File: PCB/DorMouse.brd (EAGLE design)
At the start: 40.9 x 69.4 mm, 56 parts, among them IC1 LM340MP-05, IC2 MAX1551, U1 STM32F10XRXT6, X1 MINI-USB-UX60-MB-5ST

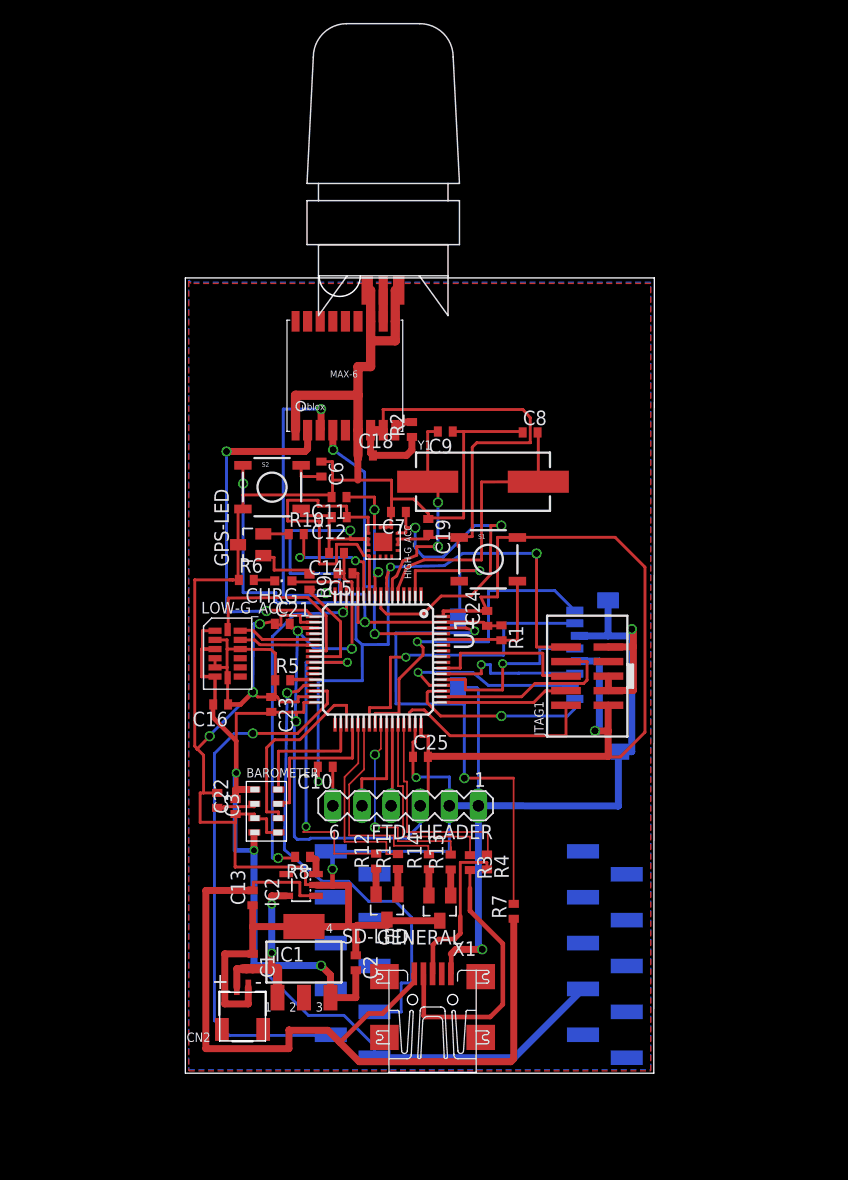
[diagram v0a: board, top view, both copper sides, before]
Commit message: Silkscreen work: values and mice
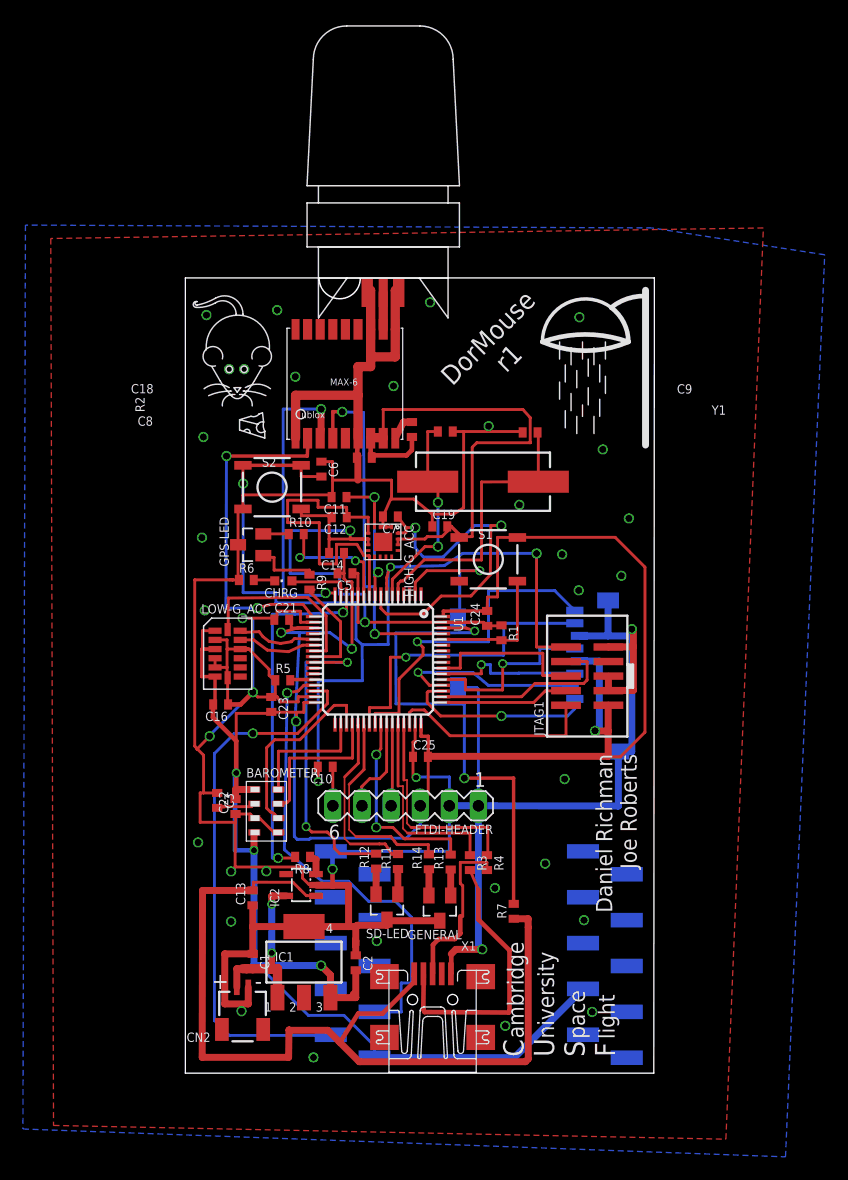
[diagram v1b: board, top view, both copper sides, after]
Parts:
- added U$2: (no value), DorMouse:SHOWER
- added U$3: (no value), DorMouse:DORMOUSE
- BAROMETER: device Swallow:LGA-8 -> DorMouse:LGA-8
- HIGH-G_ACC: device Swallow:LFCSP-16 -> DorMouse:LFCSP-16
- moved C19 1.00 mm to (22.2, 47.7), turned to 0 degrees
- moved C7 0.81 mm to (17.9, 48.6)
- moved GPS 0.70 mm to (14.0, 60.3)
- moved C21 0.36 mm to (8.41, 39.6)
- moved C18 0.22 mm to (15.6, 53.7)
- moved U$1 0.20 mm to (17.3, 68.1)
- moved R4 0.06 mm to (26.3, 18.4)
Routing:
- net TIMEPULSE: track 26.1 -> 31.2 mm
- net RESET: track 81.5 -> 86.6 mm
- net USB-5V: track 76.7 -> 81.0 mm
- net VCC: track 307.3 -> 311.0 mm
- net GND: track 382.5 -> 386.2 mm, vias 9 -> 38
- net SD_:): track 30.1 -> 28.6 mm
- net SERGEANT_SAD_FACE: track 18.8 -> 17.4 mm
- net CHARGING(-): track 30.1 -> 31.3 mm
- net ADC2: track 13.3 -> 14.4 mm
- net U1-TX: track 9.25 -> 8.48 mm
- net U2-TX: track 26.2 -> 26.9 mm
- net N$6: track 18.9 -> 18.3 mm
- net SD_:(: track 16.5 -> 15.9 mm
- net SD-DET: track 13.8 -> 13.2 mm
- net N$15: track 1.74 -> 2.32 mm
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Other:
- board text added: "C U S F"
- board text added: "Daniel Richman Joe Roberts"
- board text added: "DorMouse r1"
- board text added: "ambridge"
- board text added: "light"
- board text added: "niversity"
- board text added: "pace"

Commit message: CUSF Logo
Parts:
- added U$4: (no value), jonsowman:CUSF_LOGO
- moved R7 6.07 mm to (28.6, 20.2)
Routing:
- net N$21: track 43.7 -> 37.6 mm
- net USB-5V: track 81.0 -> 86.0 mm
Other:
- board text removed: "C U S F"
- board text removed: "ambridge"
- board text removed: "light"
- board text removed: "niversity"
- board text removed: "pace"
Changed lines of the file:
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@@
 <layer number="20" name="Dimension" color="15" fill="1" visible="yes" active="yes"/>
 <layer number="21" name="tPlace" color="7" fill="1" visible="yes" active="yes"/>
-<layer number="22" name="bPlace" color="7" fill="1" visible="yes" active="yes"/>
+<layer number="22" name="bPlace" color="7" fill="1" visible="no" active="yes"/>
 <layer number="23" name="tOrigins" color="15" fill="1" visible="yes" active="yes"/>
-<layer number="24" name="bOrigins" color="15" fill="1" visible="yes" active="yes"/>
+<layer number="24" name="bOrigins" color="15" fill="1" visible="no" active="yes"/>
 <layer number="25" name="tNames" color="7" fill="1" visible="no" active="yes"/>
 <layer number="26" name="bNames" color="7" fill="1" visible="no" active="yes"/>
@@
 <text x="27.280415625" y="63.29029375" size="1.6764" layer="21" font="vector" rot="R45" align="center">DorMouse
 r1</text>
-<text x="37.51" y="1.43" size="1.778" layer="21" font="vector" ratio="17" rot="R90">C
-U
-S
-F</text>
-<text x="29.52" y="3.05" size="1.4224" layer="21" font="vector" rot="R90">ambridge</text>
-<text x="32.17" y="3.03" size="1.4224" layer="21" font="vector" rot="R90">niversity</text>
-<text x="34.86" y="3" size="1.4224" layer="21" font="vector" rot="R90">pace</text>
-<text x="37.46" y="2.98" size="1.4224" layer="21" font="vector" rot="R90">light</text>
-<text x="39.38" y="27.85" size="1.4224" layer="21" font="vector" ratio="11" rot="R90" align="bottom-right">Daniel Richman
+<text x="27.326565625" y="14.767278125" size="1.4224" layer="21" font="vector" ratio="11" rot="R135" align="bottom-right">Daniel Richman
 Joe Roberts</text>
 </plain>
@@
 <attribute name="VALUE" x="4.525" y="41.785" size="0.6096" layer="27" font="vector"/>
 </element>
-<element name="R7" library="rcl" package="R0402" value="10k" x="28.65" y="14.12" smashed="yes" rot="R90">
-<attribute name="NAME" x="28.015" y="13.485" size="0.8128" layer="25" font="vector" rot="R90"/>
-<attribute name="VALUE" x="27.905" y="13.225" size="0.8128" layer="27" font="vector" rot="R90"/>
+<element name="R7" library="rcl" package="R0402" value="10k" x="28.65" y="20.19" smashed="yes" rot="R90">
+<attribute name="NAME" x="28.015" y="19.555" size="0.8128" layer="25" font="vector" rot="R90"/>
+<attribute name="VALUE" x="27.905" y="19.295" size="0.8128" layer="27" font="vector" rot="R90"/>
 </element>
 <element name="C14" library="rcl" package="C0402" value="1uF" x="13.19" y="45.38" smashed="yes" rot="R180">
@@
 <element name="U$2" library="DorMouse" package="SHOWER" value="" x="34.65" y="65.8"/>
 <element name="U$3" library="DorMouse" package="DORMOUSE" value="" x="4.44" y="62.43"/>
+<element name="U$4" library="jonsowman" package="CUSF_LOGO" value="" x="26.26" y="28.23" rot="R270"/>
 </elements>
 <signals>
@@
 <via x="27.01" y="16.15" extent="1-16" drill="0.6" shape="octagon"/>
 <via x="31.39" y="18.28" extent="1-16" drill="0.6" shape="octagon"/>
-<via x="35.49" y="5.34" extent="1-16" drill="0.6" shape="octagon"/>
+<via x="38.21" y="7.31" extent="1-16" drill="0.6" shape="octagon"/>
 <via x="34.78" y="13.35" extent="1-16" drill="0.6" shape="octagon"/>
 <via x="33.09" y="25.66" extent="1-16" drill="0.6" shape="octagon"/>
@@
 <contactref element="X1" pad="1"/>
 <contactref element="R7" pad="1"/>
-<wire x1="28.67" y1="13.47" x2="28.65" y2="13.47" width="0.254" layer="1"/>
+<wire x1="28.67" y1="19.48" x2="28.65" y2="19.54" width="0.254" layer="1"/>
 <contactref element="C13" pad="2"/>
 <wire x1="29.92" y1="1.25" x2="29.91" y2="12.72" width="0.6096" layer="1"/>
 <wire x1="29.91" y1="12.72" x2="29.91" y2="13.47" width="0.6096" layer="1"/>
-<wire x1="29.91" y1="13.47" x2="28.65" y2="13.47" width="0.6096" layer="1"/>
+<wire x1="29.91" y1="13.47" x2="28.65" y2="19.54" width="0.6096" layer="1"/>
 <wire x1="9.01" y1="1.38" x2="9.04" y2="3.77" width="0.6096" layer="1"/>
 <wire x1="9.01" y1="1.38" x2="1.47" y2="1.38" width="0.6096" layer="1"/>
@@
 <wire x1="28.64" y1="25.74" x2="24.34" y2="25.74" width="0.3048" layer="1"/>
 <wire x1="24.34" y1="25.74" x2="24.34" y2="32.19" width="0.254" layer="16"/>
-<wire x1="28.64" y1="14.77" x2="28.64" y2="25.74" width="0.3048" layer="1"/>
-<wire x1="28.65" y1="14.77" x2="28.64" y2="14.77" width="0.254" layer="1"/>
+<wire x1="28.64" y1="20.84" x2="28.64" y2="25.74" width="0.3048" layer="1"/>
+<wire x1="28.65" y1="20.84" x2="28.64" y2="20.84" width="0.254" layer="1"/>
 </signal>
 <signal name="N$13">

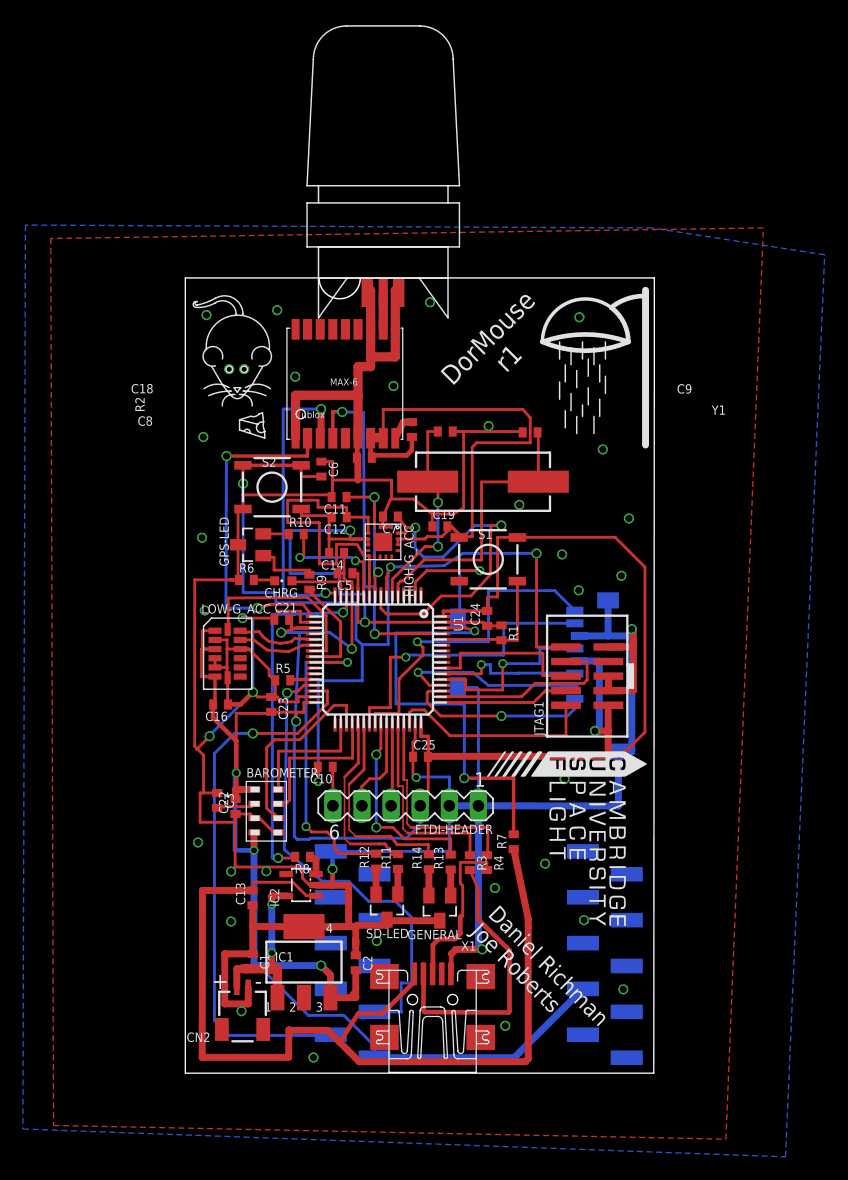
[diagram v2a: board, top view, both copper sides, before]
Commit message: Add mounting holes
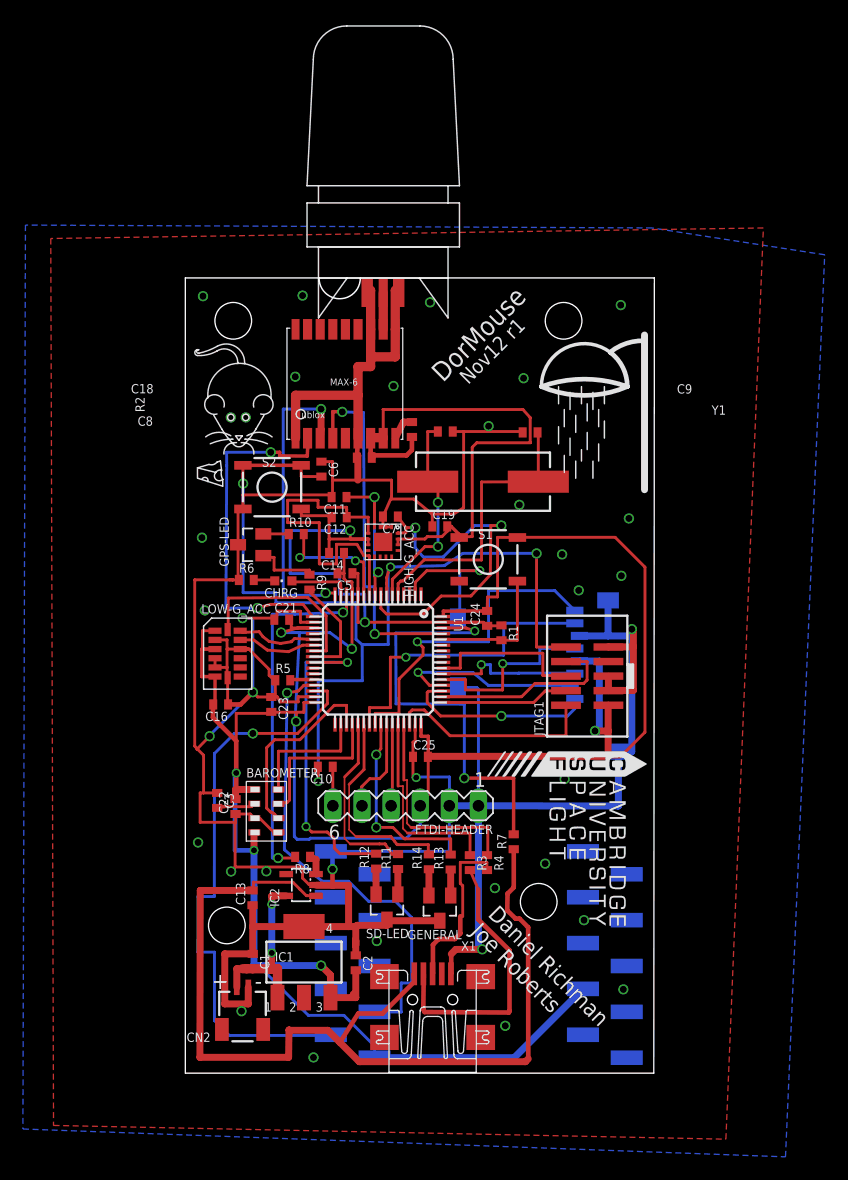
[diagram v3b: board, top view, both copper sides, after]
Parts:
- moved U$3 4.20 mm to (4.58, 58.2)
- moved U$2 3.90 mm to (34.6, 61.9)
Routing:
- net U3-RX: track 48.0 -> 50.9 mm
- net USB-5V: track 86.0 -> 87.4 mm
- net U2-RX: track 30.0 -> 30.6 mm
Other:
- board text added: "DorMouse"
- board text added: "Nov12 r1"
- board text removed: "DorMouse r1"
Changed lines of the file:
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@@
 <layer number="20" name="Dimension" color="15" fill="1" visible="yes" active="yes"/>
 <layer number="21" name="tPlace" color="7" fill="1" visible="yes" active="yes"/>
-<layer number="22" name="bPlace" color="7" fill="1" visible="no" active="yes"/>
+<layer number="22" name="bPlace" color="7" fill="1" visible="yes" active="yes"/>
 <layer number="23" name="tOrigins" color="15" fill="1" visible="yes" active="yes"/>
 <layer number="24" name="bOrigins" color="15" fill="1" visible="no" active="yes"/>
@@
 <layer number="43" name="vRestrict" color="2" fill="10" visible="yes" active="yes"/>
 <layer number="44" name="Drills" color="7" fill="1" visible="no" active="yes"/>
-<layer number="45" name="Holes" color="7" fill="1" visible="no" active="yes"/>
+<layer number="45" name="Holes" color="7" fill="1" visible="yes" active="yes"/>
 <layer number="46" name="Milling" color="3" fill="1" visible="no" active="yes"/>
 <layer number="47" name="Measures" color="7" fill="1" visible="no" active="yes"/>
@@
 <wire x1="40.92" y1="69.38" x2="0" y2="69.38" width="0" layer="20"/>
 <wire x1="0" y1="69.38" x2="0" y2="0" width="0" layer="20"/>
-<text x="27.280415625" y="63.29029375" size="1.6764" layer="21" font="vector" rot="R45" align="center">DorMouse
-r1</text>
+<text x="25.570415625" y="64.49029375" size="1.6764" layer="21" font="vector" rot="R45" align="center">DorMouse</text>
 <text x="27.326565625" y="14.767278125" size="1.4224" layer="21" font="vector" ratio="11" rot="R135" align="bottom-right">Daniel Richman
 Joe Roberts</text>
+<text x="26.770415625" y="63.02029375" size="1.27" layer="21" font="vector" rot="R45" align="center">Nov12 r1</text>
+<hole x="33" y="65.64" drill="3.2"/>
+<hole x="4.18" y="65.64" drill="3.2"/>
+<hole x="3.62" y="12.89" drill="3.2"/>
+<hole x="30.83" y="14.95" drill="3.2"/>
 </plain>
 <attributes>
@@
 <attribute name="VALUE" x="8.975" y="19.575" size="0.8128" layer="27" font="vector"/>
 </element>
-<element name="U$2" library="DorMouse" package="SHOWER" value="" x="34.65" y="65.8"/>
-<element name="U$3" library="DorMouse" package="DORMOUSE" value="" x="4.44" y="62.43"/>
+<element name="U$2" library="DorMouse" package="SHOWER" value="" x="34.56" y="61.9"/>
+<element name="U$3" library="DorMouse" package="DORMOUSE" value="" x="4.58" y="58.23"/>
 <element name="U$4" library="jonsowman" package="CUSF_LOGO" value="" x="26.26" y="28.23" rot="R270"/>
 </elements>
@@
 <wire x1="5.54" y1="37" x2="5.391971875" y2="37" width="0.254" layer="1"/>
 <wire x1="5.391971875" y1="37" x2="5.389275" y2="36.997303125" width="0.254" layer="1"/>
-<via x="1.84" y="66.14" extent="1-16" drill="0.6"/>
-<via x="8.01" y="66.57" extent="1-16" drill="0.6"/>
+<via x="1.54" y="67.79" extent="1-16" drill="0.6"/>
+<via x="10.23" y="67.84" extent="1-16" drill="0.6"/>
 <via x="21.35" y="67.25" extent="1-16" drill="0.6"/>
-<via x="34.38" y="65.95" extent="1-16" drill="0.6"/>
-<via x="36.42" y="54.42" extent="1-16" drill="0.6"/>
+<via x="37.99" y="67.01" extent="1-16" drill="0.6"/>
+<via x="29.51" y="60.63" extent="1-16" drill="0.6"/>
 <via x="26.46" y="56.45" extent="1-16" drill="0.6"/>
 <via x="18.16" y="59.95" extent="1-16" drill="0.6"/>
@@
 <via x="38.04" y="43.39" extent="1-16" drill="0.6"/>
 <via x="34.32" y="42.12" extent="1-16" drill="0.6"/>
-<via x="1.57" y="55.5" extent="1-16" drill="0.6"/>
 <via x="1.45" y="46.72" extent="1-16" drill="0.6"/>
 <via x="1.7" y="40.37" extent="1-16" drill="0.6"/>
@@
 <via x="3.99" y="17.6" extent="1-16" drill="0.6"/>
 <via x="7.07" y="17.61" extent="1-16" drill="0.6"/>
-<via x="3.99" y="13.23" extent="1-16" drill="0.6"/>
 <via x="4.9" y="5.41" extent="1-16" drill="0.6"/>
 <via x="11.18" y="1.37" extent="1-16" drill="0.6"/>
@@
 <via x="34.78" y="13.35" extent="1-16" drill="0.6" shape="octagon"/>
 <via x="33.09" y="25.66" extent="1-16" drill="0.6" shape="octagon"/>
+<via x="3.97" y="57.21" extent="1-16" drill="0.6"/>
+<via x="5.27" y="57.21" extent="1-16" drill="0.6"/>
 </signal>
 <signal name="VCC">
@@
 <wire x1="7.43" y1="40.9" x2="6.29" y2="40.58" width="0.254" layer="1"/>
 <via x="6.29" y="40.58" extent="1-16" drill="0.6" shape="octagon"/>
-<via x="3.59" y="53.84" extent="1-16" drill="0.6" shape="octagon"/>
+<via x="7.45" y="54.17" extent="1-16" drill="0.6" shape="octagon"/>
 <wire x1="6.29" y1="40.58" x2="3.54" y2="40.57" width="0.254" layer="16"/>
-<wire x1="3.54" y1="40.57" x2="3.59" y2="53.84" width="0.254" layer="16"/>
-<wire x1="3.59" y1="53.84" x2="10.64" y2="53.84" width="0.3048" layer="1"/>
+<wire x1="3.54" y1="40.57" x2="3.61" y2="53.02" width="0.254" layer="16"/>
+<wire x1="3.61" y1="53.02" x2="3.6" y2="54.17" width="0.254" layer="16"/>
+<wire x1="3.6" y1="54.17" x2="7.45" y2="54.17" width="0.254" layer="16"/>
+<wire x1="7.45" y1="54.17" x2="8.23" y2="54.17" width="0.3048" layer="1"/>
+<wire x1="8.23" y1="54.17" x2="8.23" y2="53.85" width="0.3048" layer="1"/>
+<wire x1="8.23" y1="53.85" x2="10.64" y2="53.84" width="0.3048" layer="1"/>
 <wire x1="10.64" y1="53.84" x2="10.666" y2="54.466" width="0.3048" layer="1"/>
 <wire x1="10.666" y1="54.466" x2="10.666" y2="55.394" width="0.3048" layer="1"/>
@@
 <wire x1="28.67" y1="19.48" x2="28.65" y2="19.54" width="0.254" layer="1"/>
 <contactref element="C13" pad="2"/>
-<wire x1="29.92" y1="1.25" x2="29.91" y2="12.72" width="0.6096" layer="1"/>
-<wire x1="29.91" y1="12.72" x2="29.91" y2="13.47" width="0.6096" layer="1"/>
-<wire x1="29.91" y1="13.47" x2="28.65" y2="19.54" width="0.6096" layer="1"/>
+<wire x1="29.92" y1="1.25" x2="29.91" y2="12.72" width="0.4064" layer="1"/>
+<wire x1="29.91" y1="12.72" x2="29.16003125" y2="13.47688125" width="0.4064" layer="1"/>
+<wire x1="29.16003125" y1="13.47688125" x2="28.82" y2="13.48" width="0.4064" layer="1"/>
+<wire x1="28.82" y1="13.48" x2="28.08353125" y2="14.190984375" width="0.4064" layer="1"/>
+<wire x1="28.08353125" y1="14.190984375" x2="28.11" y2="15.66" width="0.4064" layer="1"/>
+<wire x1="28.11" y1="15.66" x2="28.65" y2="16.2" width="0.4064" layer="1"/>
+<wire x1="28.65" y1="16.2" x2="28.65" y2="19.54" width="0.4064" layer="1"/>
 <wire x1="9.01" y1="1.38" x2="9.04" y2="3.77" width="0.6096" layer="1"/>
-<wire x1="9.01" y1="1.38" x2="1.47" y2="1.38" width="0.6096" layer="1"/>
-<wire x1="1.5" y1="15.94" x2="1.47" y2="1.38" width="0.6096" layer="1"/>
-<wire x1="1.5" y1="15.94" x2="5.86" y2="15.94" width="0.6096" layer="1"/>
+<wire x1="9.01" y1="1.38" x2="1.27" y2="1.38" width="0.6096" layer="1"/>
+<wire x1="1.3" y1="15.94" x2="1.27" y2="1.38" width="0.6096" layer="1"/>
+<wire x1="1.3" y1="15.94" x2="5.86" y2="15.94" width="0.6096" layer="1"/>
 <wire x1="5.86" y1="15.94" x2="5.86" y2="15.95" width="0.6096" layer="1"/>
 <wire x1="5.86" y1="15.95" x2="5.94" y2="15.95" width="0.6096" layer="1"/>
@@
 <wire x1="12.632" y1="3.29" x2="3.84" y2="3.29" width="0.254" layer="16"/>
 <wire x1="3.84" y1="3.29" x2="2.54" y2="4.59" width="0.254" layer="16"/>
-<wire x1="2.54" y1="4.59" x2="2.54" y2="27.89" width="0.254" layer="16"/>
+<wire x1="2.54" y1="4.59" x2="2.54" y2="10.56" width="0.254" layer="16"/>
+<wire x1="2.54" y1="10.56" x2="1.1" y2="10.56" width="0.254" layer="16"/>
+<wire x1="1.1" y1="10.56" x2="1.1" y2="15.41" width="0.254" layer="16"/>
+<wire x1="1.1" y1="15.41" x2="2.53" y2="15.41" width="0.254" layer="16"/>
+<wire x1="2.53" y1="15.41" x2="2.54" y2="27.89" width="0.254" layer="16"/>
 <wire x1="2.54" y1="27.89" x2="4.29" y2="29.64" width="0.254" layer="16"/>
 <wire x1="4.29" y1="29.64" x2="5.89" y2="29.64" width="0.254" layer="16"/>
@@
 <wire x1="11.4" y1="18.65" x2="11.4" y2="17.37" width="0.6096" layer="1"/>
 </signal>
-<signal name="N$22">
-<via x="3.82" y="61.42" extent="1-16" drill="0.6"/>
-</signal>
-<signal name="N$25">
-<via x="5.13" y="61.42" extent="1-16" drill="0.6"/>
-</signal>
 </signals>
